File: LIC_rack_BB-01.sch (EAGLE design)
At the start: 25 parts, among them IC1 74HC125D, IC3 74HC125D, IC4 MEGA128-A, IC6 MAX481CSA, Q1 14.7456, Q2 IRLL014, U1 ATPROG-V

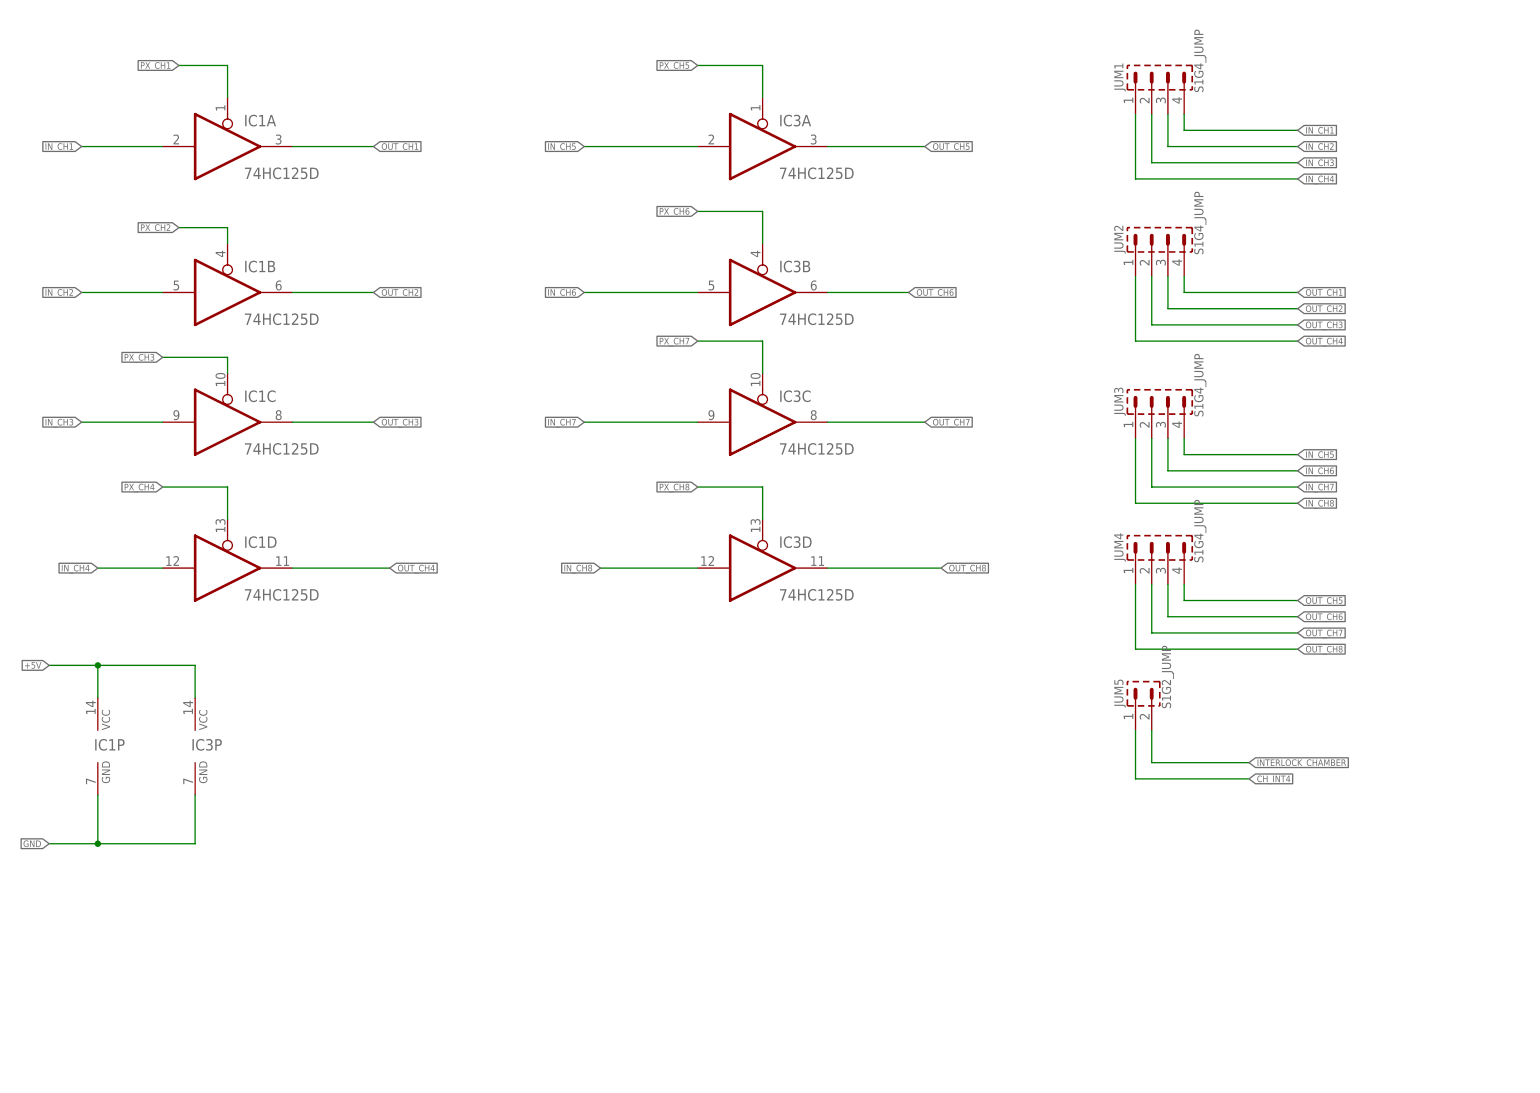
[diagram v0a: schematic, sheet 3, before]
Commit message: Pridána nová verze
Přidána nová verze zkráceno na 4 In a 4 Out a přidáno relé na desku
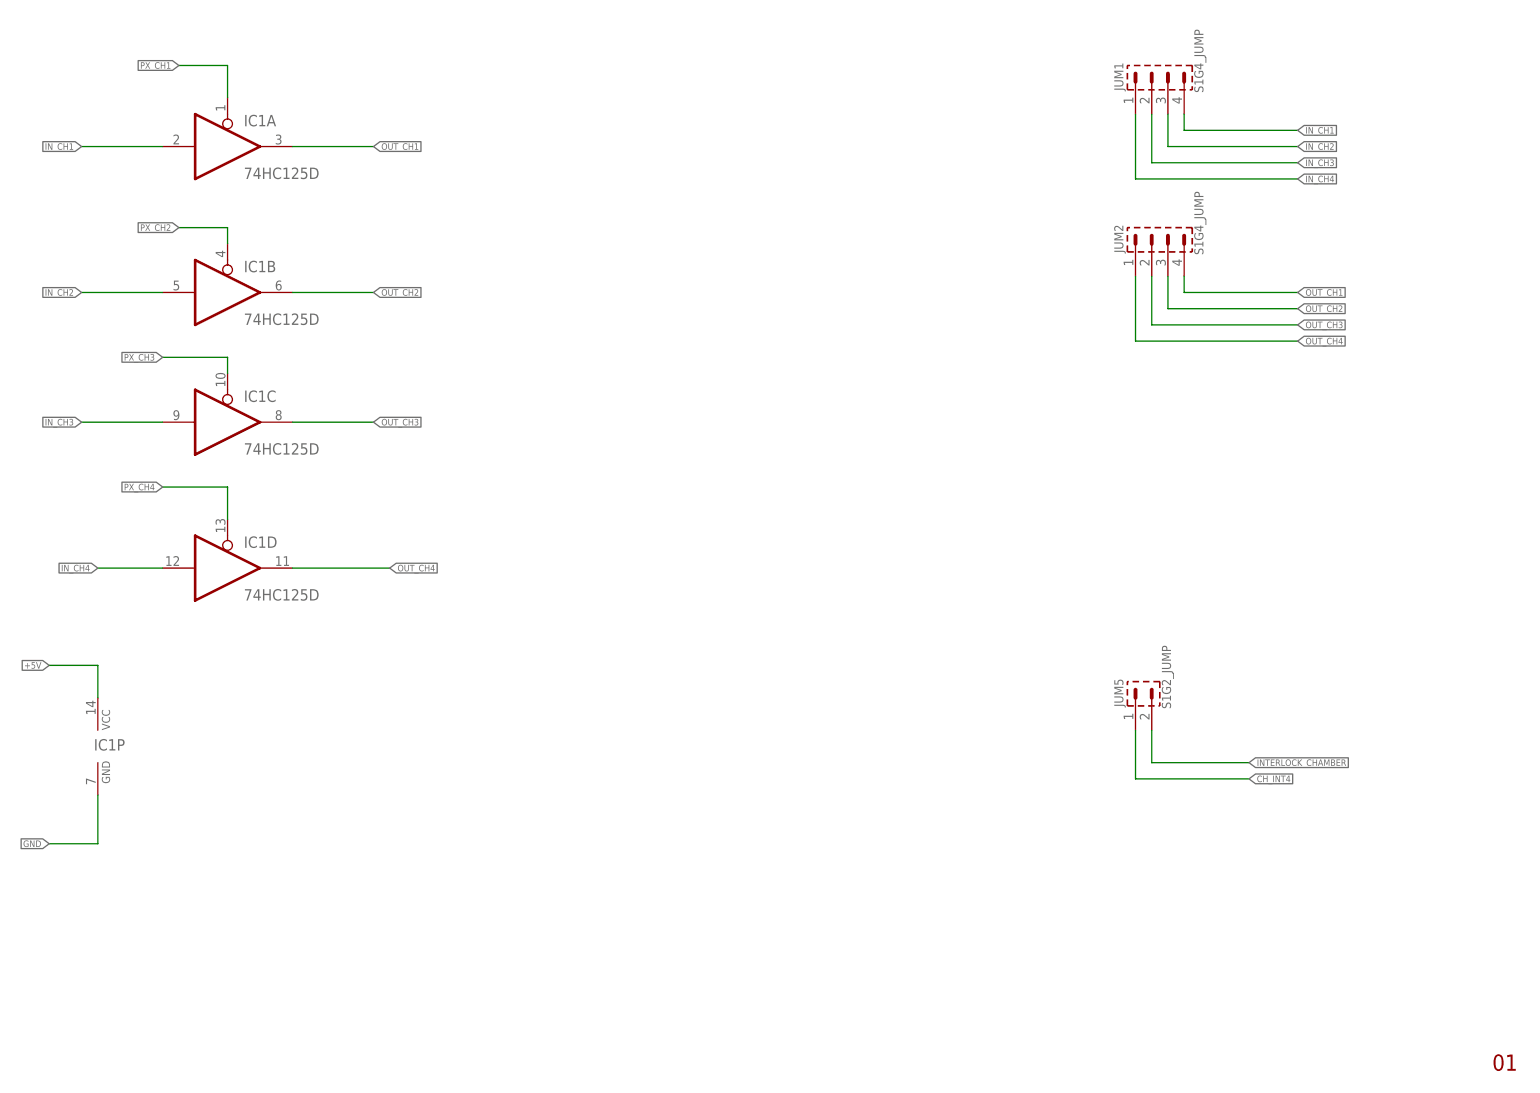
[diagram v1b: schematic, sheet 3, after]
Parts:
- removed IC3: 74HC125D, 74xx-eu:74HC125D
- removed JUM3, JUM4: S1G4_JUMP, #PaJa_konektory:S1G4_JUMP
- R6: value (none) -> 10k
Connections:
- removed net IN_CH5: IC3A.I, JUM3.4
- removed net IN_CH6: IC3B.I, JUM3.3
- removed net IN_CH7: IC3C.I, JUM3.2
- removed net IN_CH8: IC3D.I, JUM3.1
- removed net IN_LASER: REL1SPIN.1
- removed net OUT_CH5: IC3A.O, JUM4.4
- removed net OUT_CH6: IC3B.O, JUM4.3
- removed net OUT_CH7: IC3C.O, JUM4.2
- removed net OUT_CH8: IC3D.O, JUM4.1
- removed net PA7: Q2.G, R6.2
- new net OUT_LASER: J1-A22.MS, REL1SPIN.1
- net +5V: now also R1.1, R3.1, R4.1; no longer IC3P.VCC
- net GND: no longer IC3P.GND, R1.1, R3.1, R4.1
- net PX_CH5: now also Q2.G, R6.2; no longer IC3A.OE, J1-A22.MS
- net PX_CH6: no longer IC3B.OE
- net PX_CH7: no longer IC3C.OE
- net PX_CH8: no longer IC3D.OE
- net PX_MISO: no longer U1.MISO
- net PX_MOSI: no longer U1.MOSI
- net SYS_RX: now also U1.MOSI
- net SYS_TX: now also U1.MISO
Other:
- note added: "01"
- moved on the sheet: R4
